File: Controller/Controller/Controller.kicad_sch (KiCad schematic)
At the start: 59 parts, among them Q2 2N5457, Q3 2N5457, U2 TL072, U3 LF444, U4 TL074, U5 TL074, U6 TL072

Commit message: controller almost routed
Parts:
- C3: value 100nF -> 4.7nF
- D1: renamed from D5; footprint Diode_THT:D_DO-35_SOD27_P7.62mm_Horizontal -> Diode_THT:D_T-1_P5.08mm_Horizontal
- D10, D11, D4, D6, D7: footprint Diode_THT:D_DO-35_SOD27_P7.62mm_Horizontal -> Diode_THT:D_T-1_P5.08mm_Horizontal
- D2: renamed from D1; footprint Diode_THT:D_DO-35_SOD27_P7.62mm_Horizontal -> Diode_THT:D_T-1_P5.08mm_Horizontal
- D3: renamed from D2; footprint Diode_THT:D_DO-35_SOD27_P7.62mm_Horizontal -> Diode_THT:D_T-1_P5.08mm_Horizontal
- D5: renamed from D3; footprint Diode_THT:D_DO-35_SOD27_P7.62mm_Horizontal -> Diode_THT:D_T-1_P5.08mm_Horizontal
- D8: renamed from D9; footprint Diode_THT:D_DO-35_SOD27_P7.62mm_Horizontal -> Diode_THT:D_T-1_P5.08mm_Horizontal
- D9: renamed from D8; footprint Diode_THT:D_DO-35_SOD27_P7.62mm_Horizontal -> Diode_THT:D_T-1_P5.08mm_Horizontal
- R1: value 1M -> 100K
- R1: value 10k -> 100k
- R1: value 1M -> 300K
- renumbered Q3 to Q1, U5 to U1, U4 to U2, U2 to U3, U3 to U4, U6 to U5

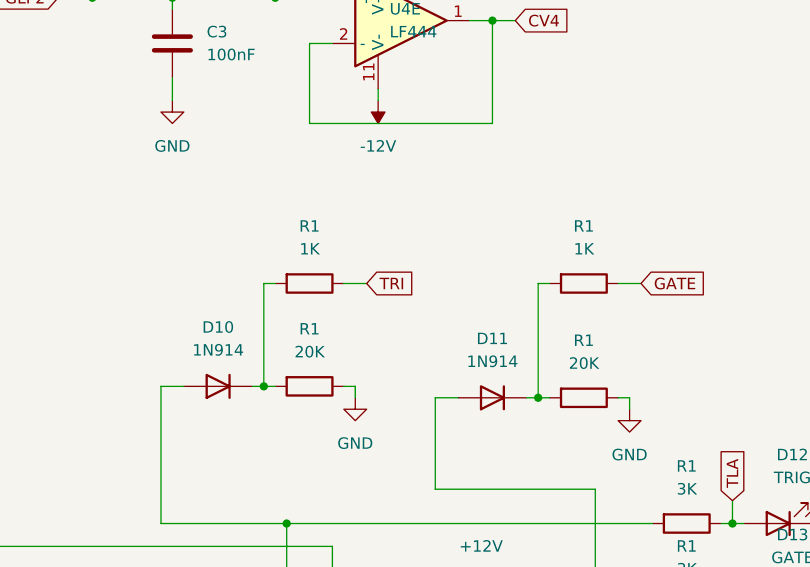
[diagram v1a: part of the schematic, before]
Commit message: controller - changed resistor sizes
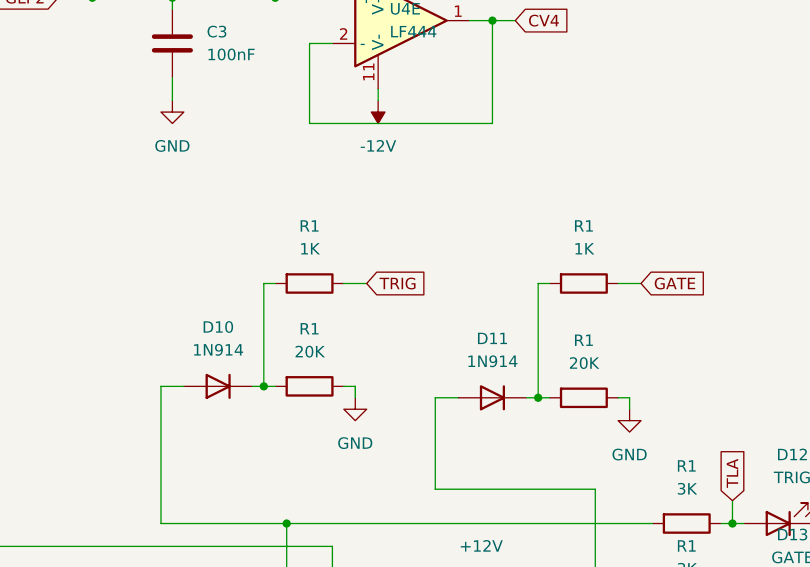
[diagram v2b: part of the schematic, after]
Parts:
- C8: footprint Capacitor_THT:CP_Radial_D4.0mm_P2.00mm -> Capacitor_THT:CP_Radial_D5.0mm_P2.50mm
- R1: footprint Resistor_THT:R_Axial_DIN0204_L3.6mm_D1.6mm_P5.08mm_Horizontal -> Resistor_THT:R_Axial_DIN0207_L6.3mm_D2.5mm_P7.62mm_Horizontal
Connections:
- net TRI renamed TRIG

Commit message: minor cleanup
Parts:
- R1: footprint Resistor_THT:R_Axial_DIN0207_L6.3mm_D2.5mm_P7.62mm_Horizontal -> Library:R_Axial_DIN0207_L6.3mm_D2.5mm_P7.62mm_Horizontal
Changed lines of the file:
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@@
       (effects (font (size 1.27 1.27)) (justify left))
     )
-    (property "Footprint" "Resistor_THT:R_Axial_DIN0207_L6.3mm_D2.5mm_P7.62mm_Horizontal" (at 130.302 127 90)
+    (property "Footprint" "Library:R_Axial_DIN0207_L6.3mm_D2.5mm_P7.62mm_Horizontal" (at 130.302 127 90)
       (effects (font (size 1.27 1.27)) hide)
     )
@@
       (effects (font (size 1.27 1.27)))
     )
-    (property "Footprint" "Resistor_THT:R_Axial_DIN0207_L6.3mm_D2.5mm_P7.62mm_Horizontal" (at 72.39 111.252 90)
+    (property "Footprint" "Library:R_Axial_DIN0207_L6.3mm_D2.5mm_P7.62mm_Horizontal" (at 72.39 111.252 90)
       (effects (font (size 1.27 1.27)) hide)
     )
@@
       (effects (font (size 1.27 1.27)))
     )
-    (property "Footprint" "Resistor_THT:R_Axial_DIN0207_L6.3mm_D2.5mm_P7.62mm_Horizontal" (at 210.82 117.602 90)
+    (property "Footprint" "Library:R_Axial_DIN0207_L6.3mm_D2.5mm_P7.62mm_Horizontal" (at 210.82 117.602 90)
       (effects (font (size 1.27 1.27)) hide)
     )
@@
       (effects (font (size 1.27 1.27)))
     )
-    (property "Footprint" "Resistor_THT:R_Axial_DIN0207_L6.3mm_D2.5mm_P7.62mm_Horizontal" (at 71.12 181.102 90)
+    (property "Footprint" "Library:R_Axial_DIN0207_L6.3mm_D2.5mm_P7.62mm_Horizontal" (at 71.12 181.102 90)
       (effects (font (size 1.27 1.27)) hide)
     )
@@
       (effects (font (size 1.27 1.27)))
     )
-    (property "Footprint" "Resistor_THT:R_Axial_DIN0207_L6.3mm_D2.5mm_P7.62mm_Horizontal" (at 241.3 106.172 90)
+    (property "Footprint" "Library:R_Axial_DIN0207_L6.3mm_D2.5mm_P7.62mm_Horizontal" (at 241.3 106.172 90)
       (effects (font (size 1.27 1.27)) hide)
     )
@@
       (effects (font (size 1.27 1.27)) (justify left))
     )
-    (property "Footprint" "Resistor_THT:R_Axial_DIN0207_L6.3mm_D2.5mm_P7.62mm_Horizontal" (at 61.722 127 90)
+    (property "Footprint" "Library:R_Axial_DIN0207_L6.3mm_D2.5mm_P7.62mm_Horizontal" (at 61.722 127 90)
       (effects (font (size 1.27 1.27)) hide)
     )
@@
       (effects (font (size 1.27 1.27)))
     )
-    (property "Footprint" "Resistor_THT:R_Axial_DIN0207_L6.3mm_D2.5mm_P7.62mm_Horizontal" (at 125.73 82.042 90)
+    (property "Footprint" "Library:R_Axial_DIN0207_L6.3mm_D2.5mm_P7.62mm_Horizontal" (at 125.73 82.042 90)
       (effects (font (size 1.27 1.27)) hide)
     )
@@
       (effects (font (size 1.27 1.27)))
     )
-    (property "Footprint" "Resistor_THT:R_Axial_DIN0207_L6.3mm_D2.5mm_P7.62mm_Horizontal" (at 31.75 187.452 90)
+    (property "Footprint" "Library:R_Axial_DIN0207_L6.3mm_D2.5mm_P7.62mm_Horizontal" (at 31.75 187.452 90)
       (effects (font (size 1.27 1.27)) hide)
     )
@@
       (effects (font (size 1.27 1.27)))
     )
-    (property "Footprint" "Resistor_THT:R_Axial_DIN0207_L6.3mm_D2.5mm_P7.62mm_Horizontal" (at 252.73 141.732 90)
+    (property "Footprint" "Library:R_Axial_DIN0207_L6.3mm_D2.5mm_P7.62mm_Horizontal" (at 252.73 141.732 90)
       (effects (font (size 1.27 1.27)) hide)
     )
@@
       (effects (font (size 1.27 1.27)) (justify left))
     )
-    (property "Footprint" "Resistor_THT:R_Axial_DIN0207_L6.3mm_D2.5mm_P7.62mm_Horizontal" (at 120.142 185.42 90)
+    (property "Footprint" "Library:R_Axial_DIN0207_L6.3mm_D2.5mm_P7.62mm_Horizontal" (at 120.142 185.42 90)
       (effects (font (size 1.27 1.27)) hide)
     )
@@
       (effects (font (size 1.27 1.27)))
     )
-    (property "Footprint" "Resistor_THT:R_Axial_DIN0207_L6.3mm_D2.5mm_P7.62mm_Horizontal" (at 111.76 92.202 90)
+    (property "Footprint" "Library:R_Axial_DIN0207_L6.3mm_D2.5mm_P7.62mm_Horizontal" (at 111.76 92.202 90)
       (effects (font (size 1.27 1.27)) hide)
     )
@@
       (effects (font (size 1.27 1.27)))
     )
-    (property "Footprint" "Resistor_THT:R_Axial_DIN0207_L6.3mm_D2.5mm_P7.62mm_Horizontal" (at 55.88 104.902 90)
+    (property "Footprint" "Library:R_Axial_DIN0207_L6.3mm_D2.5mm_P7.62mm_Horizontal" (at 55.88 104.902 90)
       (effects (font (size 1.27 1.27)) hide)
     )
@@
       (effects (font (size 1.27 1.27)))
     )
-    (property "Footprint" "Resistor_THT:R_Axial_DIN0207_L6.3mm_D2.5mm_P7.62mm_Horizontal" (at 210.82 106.172 90)
+    (property "Footprint" "Library:R_Axial_DIN0207_L6.3mm_D2.5mm_P7.62mm_Horizontal" (at 210.82 106.172 90)
       (effects (font (size 1.27 1.27)) hide)
     )
@@
       (effects (font (size 1.27 1.27)) (justify left))
     )
-    (property "Footprint" "Resistor_THT:R_Axial_DIN0207_L6.3mm_D2.5mm_P7.62mm_Horizontal" (at 98.552 185.42 90)
+    (property "Footprint" "Library:R_Axial_DIN0207_L6.3mm_D2.5mm_P7.62mm_Horizontal" (at 98.552 185.42 90)
       (effects (font (size 1.27 1.27)) hide)
     )
@@
       (effects (font (size 1.27 1.27)) (justify left))
     )
-    (property "Footprint" "Resistor_THT:R_Axial_DIN0207_L6.3mm_D2.5mm_P7.62mm_Horizontal" (at 21.082 125.73 90)
+    (property "Footprint" "Library:R_Axial_DIN0207_L6.3mm_D2.5mm_P7.62mm_Horizontal" (at 21.082 125.73 90)
       (effects (font (size 1.27 1.27)) hide)
     )
@@
       (effects (font (size 1.27 1.27)) (justify left))
     )
-    (property "Footprint" "Resistor_THT:R_Axial_DIN0207_L6.3mm_D2.5mm_P7.62mm_Horizontal" (at 184.912 55.88 90)
+    (property "Footprint" "Library:R_Axial_DIN0207_L6.3mm_D2.5mm_P7.62mm_Horizontal" (at 184.912 55.88 90)
       (effects (font (size 1.27 1.27)) hide)
     )
@@
       (effects (font (size 1.27 1.27)) (justify left))
     )
-    (property "Footprint" "Resistor_THT:R_Axial_DIN0207_L6.3mm_D2.5mm_P7.62mm_Horizontal" (at 117.602 127 90)
+    (property "Footprint" "Library:R_Axial_DIN0207_L6.3mm_D2.5mm_P7.62mm_Horizontal" (at 117.602 127 90)
       (effects (font (size 1.27 1.27)) hide)
     )
@@
       (effects (font (size 1.27 1.27)) (justify left))
     )
-    (property "Footprint" "Resistor_THT:R_Axial_DIN0207_L6.3mm_D2.5mm_P7.62mm_Horizontal" (at 149.352 78.74 90)
+    (property "Footprint" "Library:R_Axial_DIN0207_L6.3mm_D2.5mm_P7.62mm_Horizontal" (at 149.352 78.74 90)
       (effects (font (size 1.27 1.27)) hide)
     )
@@
       (effects (font (size 1.27 1.27)) (justify left))
     )
-    (property "Footprint" "Resistor_THT:R_Axial_DIN0207_L6.3mm_D2.5mm_P7.62mm_Horizontal" (at 46.482 184.15 90)
+    (property "Footprint" "Library:R_Axial_DIN0207_L6.3mm_D2.5mm_P7.62mm_Horizontal" (at 46.482 184.15 90)
       (effects (font (size 1.27 1.27)) hide)
     )
@@
       (effects (font (size 1.27 1.27)) (justify left))
     )
-    (property "Footprint" "Resistor_THT:R_Axial_DIN0207_L6.3mm_D2.5mm_P7.62mm_Horizontal" (at 141.732 88.9 90)
+    (property "Footprint" "Library:R_Axial_DIN0207_L6.3mm_D2.5mm_P7.62mm_Horizontal" (at 141.732 88.9 90)
       (effects (font (size 1.27 1.27)) hide)
     )
@@
       (effects (font (size 1.27 1.27)))
     )
-    (property "Footprint" "Resistor_THT:R_Axial_DIN0207_L6.3mm_D2.5mm_P7.62mm_Horizontal" (at 38.1 116.332 90)
+    (property "Footprint" "Library:R_Axial_DIN0207_L6.3mm_D2.5mm_P7.62mm_Horizontal" (at 38.1 116.332 90)
       (effects (font (size 1.27 1.27)) hide)
     )
@@
       (effects (font (size 1.27 1.27)))
     )
-    (property "Footprint" "Resistor_THT:R_Axial_DIN0207_L6.3mm_D2.5mm_P7.62mm_Horizontal" (at 99.06 111.252 90)
+    (property "Footprint" "Library:R_Axial_DIN0207_L6.3mm_D2.5mm_P7.62mm_Horizontal" (at 99.06 111.252 90)
       (effects (font (size 1.27 1.27)) hide)
     )
@@
       (effects (font (size 1.27 1.27)))
     )
-    (property "Footprint" "Resistor_THT:R_Axial_DIN0207_L6.3mm_D2.5mm_P7.62mm_Horizontal" (at 241.3 118.872 90)
+    (property "Footprint" "Library:R_Axial_DIN0207_L6.3mm_D2.5mm_P7.62mm_Horizontal" (at 241.3 118.872 90)
       (effects (font (size 1.27 1.27)) hide)
     )
@@
       (effects (font (size 1.27 1.27)))
     )
-    (property "Footprint" "Resistor_THT:R_Axial_DIN0207_L6.3mm_D2.5mm_P7.62mm_Horizontal" (at 81.28 181.102 90)
+    (property "Footprint" "Library:R_Axial_DIN0207_L6.3mm_D2.5mm_P7.62mm_Horizontal" (at 81.28 181.102 90)
       (effects (font (size 1.27 1.27)) hide)
     )
@@
       (effects (font (size 1.27 1.27)))
     )
-    (property "Footprint" "Resistor_THT:R_Axial_DIN0207_L6.3mm_D2.5mm_P7.62mm_Horizontal" (at 44.45 71.882 90)
+    (property "Footprint" "Library:R_Axial_DIN0207_L6.3mm_D2.5mm_P7.62mm_Horizontal" (at 44.45 71.882 90)
       (effects (font (size 1.27 1.27)) hide)
     )
@@
       (effects (font (size 1.27 1.27)) (justify left))
     )
-    (property "Footprint" "Resistor_THT:R_Axial_DIN0207_L6.3mm_D2.5mm_P7.62mm_Horizontal" (at 84.582 127 90)
+    (property "Footprint" "Library:R_Axial_DIN0207_L6.3mm_D2.5mm_P7.62mm_Horizontal" (at 84.582 127 90)
       (effects (font (size 1.27 1.27)) hide)
     )
@@
       (effects (font (size 1.27 1.27)))
     )
-    (property "Footprint" "Resistor_THT:R_Axial_DIN0207_L6.3mm_D2.5mm_P7.62mm_Horizontal" (at 252.73 132.842 90)
+    (property "Footprint" "Library:R_Axial_DIN0207_L6.3mm_D2.5mm_P7.62mm_Horizontal" (at 252.73 132.842 90)
       (effects (font (size 1.27 1.27)) hide)
     )
@@
       (effects (font (size 1.27 1.27)) (justify left))
     )
-    (property "Footprint" "Resistor_THT:R_Axial_DIN0207_L6.3mm_D2.5mm_P7.62mm_Horizontal" (at 21.082 106.68 90)
+    (property "Footprint" "Library:R_Axial_DIN0207_L6.3mm_D2.5mm_P7.62mm_Horizontal" (at 21.082 106.68 90)
       (effects (font (size 1.27 1.27)) hide)
     )

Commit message: Controller - minor fixes
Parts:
- C3: footprint Capacitor_THT:C_Disc_D3.0mm_W1.6mm_P2.50mm -> Capacitor_THT:C_Radial_D8.0mm_H11.5mm_P3.50mm
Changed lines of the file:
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@@
       (effects (font (size 1.27 1.27)) (justify left))
     )
-    (property "Footprint" "Capacitor_THT:C_Disc_D3.0mm_W1.6mm_P2.50mm" (at 162.2552 87.63 0)
+    (property "Footprint" "Capacitor_THT:C_Radial_D8.0mm_H11.5mm_P3.50mm" (at 162.2552 87.63 0)
       (effects (font (size 1.27 1.27)) hide)
     )
